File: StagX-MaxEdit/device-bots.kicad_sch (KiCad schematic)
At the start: 2 parts

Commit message: Updated maxedit after git fun
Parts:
- gave numbers to parts that had none: 2
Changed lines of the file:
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@@
   (symbol (lib_id "Connectors_SUFST:Deutsch_DTM_2P_Pin") (at 154.94 97.155 180) (unit 1)
     (in_bom yes) (on_board yes) (dnp no) (fields_autoplaced)
-    (property "Reference" "Conn?" (at 160.02 89.535 0)
+    (property "Reference" "Conn8" (at 160.02 89.535 0)
       (effects (font (size 1.27 1.27)) (justify right))
     )
@@
     (instances
       (project "StagX"
-        (path "/03011643-0690-4b85-ab78-d6a62dae52b1/3cdef822-b27b-4a71-b67b-74c9f7188311"
-          (reference "Conn?") (unit 1)
-        )
-        (path "/03011643-0690-4b85-ab78-d6a62dae52b1/8cb55a6b-0d65-49e2-b083-4cc99e15786c"
-          (reference "Conn?") (unit 1)
-        )
-        (path "/03011643-0690-4b85-ab78-d6a62dae52b1/a345ed85-d8da-42e0-9850-81cfb8a2389f"
-          (reference "Conn?") (unit 1)
-        )
         (path "/03011643-0690-4b85-ab78-d6a62dae52b1/070b8217-88a3-4264-8b23-f32d97ad3850"
           (reference "Conn8") (unit 1)
@@
   (symbol (lib_id "Switch:SW_Push_Open") (at 120.015 90.17 0) (unit 1)
     (in_bom yes) (on_board yes) (dnp no) (fields_autoplaced)
-    (property "Reference" "SW?" (at 120.015 85.09 0)
+    (property "Reference" "SW1" (at 120.015 85.09 0)
       (effects (font (size 1.27 1.27)))
     )
@@
     (instances
       (project "StagX"
-        (path "/03011643-0690-4b85-ab78-d6a62dae52b1/3cdef822-b27b-4a71-b67b-74c9f7188311"
-          (reference "SW?") (unit 1)
-        )
-        (path "/03011643-0690-4b85-ab78-d6a62dae52b1/8cb55a6b-0d65-49e2-b083-4cc99e15786c"
-          (reference "SW?") (unit 1)
-        )
-        (path "/03011643-0690-4b85-ab78-d6a62dae52b1/a345ed85-d8da-42e0-9850-81cfb8a2389f"
-          (reference "SW?") (unit 1)
-        )
         (path "/03011643-0690-4b85-ab78-d6a62dae52b1/070b8217-88a3-4264-8b23-f32d97ad3850"
           (reference "SW1") (unit 1)

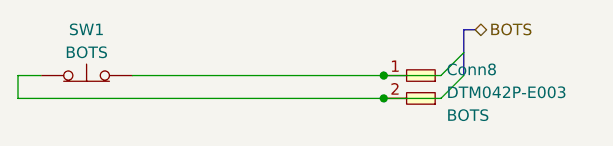
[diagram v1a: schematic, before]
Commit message: Added initial version for loom routing
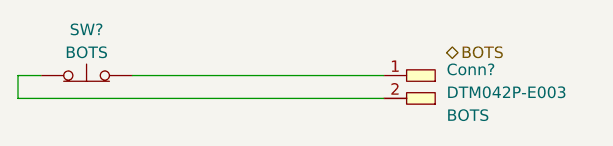
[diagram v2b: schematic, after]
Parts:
- renumbered Conn8 to Conn?, SW1 to SW?
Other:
- title: (none) -> DEVICE - BOTS
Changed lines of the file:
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@@
 (kicad_sch (version 20230121) (generator eeschema)
   (paper "A4")
-  (junction (at 153.035 90.17) (diameter 0) (color 0 0 0 0)
-  )
-  (junction (at 153.035 92.71) (diameter 0) (color 0 0 0 0)
-  )
-  (bus_entry (at 159.385 92.71) (size 2.54 -2.54)
-    (stroke (width 0) (type default))
-  )
-  (bus_entry (at 159.385 90.17) (size 2.54 -2.54)
-    (stroke (width 0) (type default))
-  )
-  (bus (pts (xy 161.925 90.17) (xy 161.925 87.63))
-    (stroke (width 0) (type default))
-  )
-  (bus (pts (xy 161.925 87.63) (xy 161.925 85.09))
-    (stroke (width 0) (type default))
-  )
-  (wire (pts (xy 153.035 90.17) (xy 159.385 90.17))
-    (stroke (width 0) (type default))
+  (title_block
+    (title "DEVICE - BOTS")
   )
   (wire (pts (xy 114.935 90.17) (xy 112.395 90.17))
@@
   )
   (wire (pts (xy 112.395 92.71) (xy 153.035 92.71))
-    (stroke (width 0) (type default))
-  )
-  (bus (pts (xy 161.925 85.09) (xy 163.195 85.09))
     (stroke (width 0) (type default))
   )
@@
     (stroke (width 0) (type default))
   )
-  (wire (pts (xy 153.035 92.71) (xy 159.385 92.71))
-    (stroke (width 0) (type default))
-  )
-  (hierarchical_label "BOTS" (shape bidirectional) (at 163.195 85.09 0) (fields_autoplaced)
+  (hierarchical_label "BOTS" (shape bidirectional) (at 160.02 87.63 0) (fields_autoplaced)
     (effects (font (size 1.27 1.27)) (justify left))
   )
   (symbol (lib_id "Connectors_SUFST:Deutsch_DTM_2P_Pin") (at 154.94 97.155 180) (unit 1)
     (in_bom yes) (on_board yes) (dnp no) (fields_autoplaced)
-    (property "Reference" "Conn8" (at 160.02 89.535 0)
+    (property "Reference" "Conn?" (at 160.02 89.535 0)
       (effects (font (size 1.27 1.27)) (justify right))
     )
@@
       (project "StagX"
         (path "/03011643-0690-4b85-ab78-d6a62dae52b1/070b8217-88a3-4264-8b23-f32d97ad3850"
-          (reference "Conn8") (unit 1)
+          (reference "Conn?") (unit 1)
         )
       )
@@
   (symbol (lib_id "Switch:SW_Push_Open") (at 120.015 90.17 0) (unit 1)
     (in_bom yes) (on_board yes) (dnp no) (fields_autoplaced)
-    (property "Reference" "SW1" (at 120.015 85.09 0)
+    (property "Reference" "SW?" (at 120.015 85.09 0)
       (effects (font (size 1.27 1.27)))
     )
@@
       (project "StagX"
         (path "/03011643-0690-4b85-ab78-d6a62dae52b1/070b8217-88a3-4264-8b23-f32d97ad3850"
-          (reference "SW1") (unit 1)
+          (reference "SW?") (unit 1)
         )
       )
